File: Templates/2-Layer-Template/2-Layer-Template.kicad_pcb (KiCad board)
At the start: 2 copper layers, 0 parts

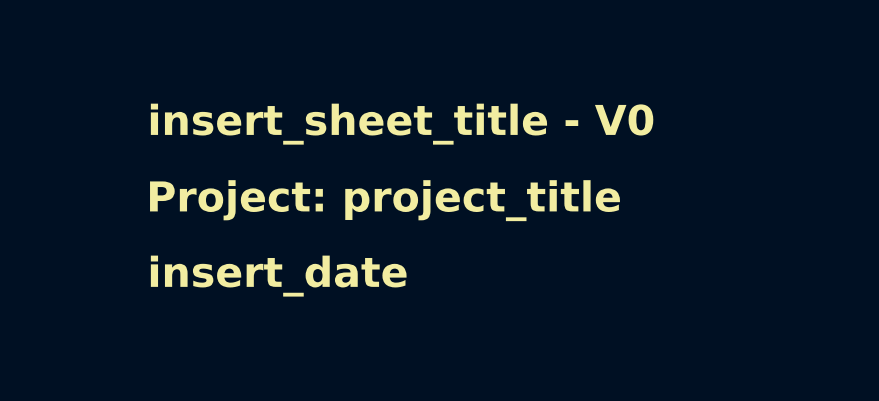
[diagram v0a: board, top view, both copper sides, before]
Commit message: Fixed template silkscreen
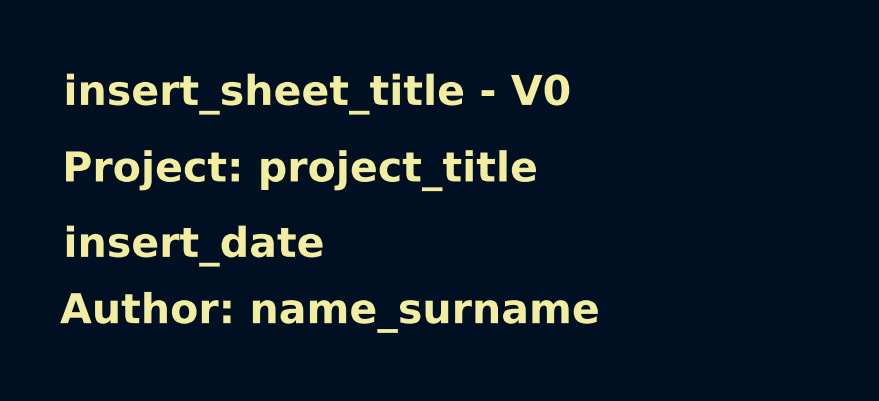
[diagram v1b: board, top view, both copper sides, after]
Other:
- board text added: "${COMMENT2}"
